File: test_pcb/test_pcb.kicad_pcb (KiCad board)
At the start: 2 copper layers, 67 parts, among them K0 KEYSW, K1 KEYSW, K10 KEYSW, K12 KEYSW, K13 KEYSW, K14 KEYSW, K15 KEYSW, K16 KEYSW, K17 KEYSW, K18 KEYSW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

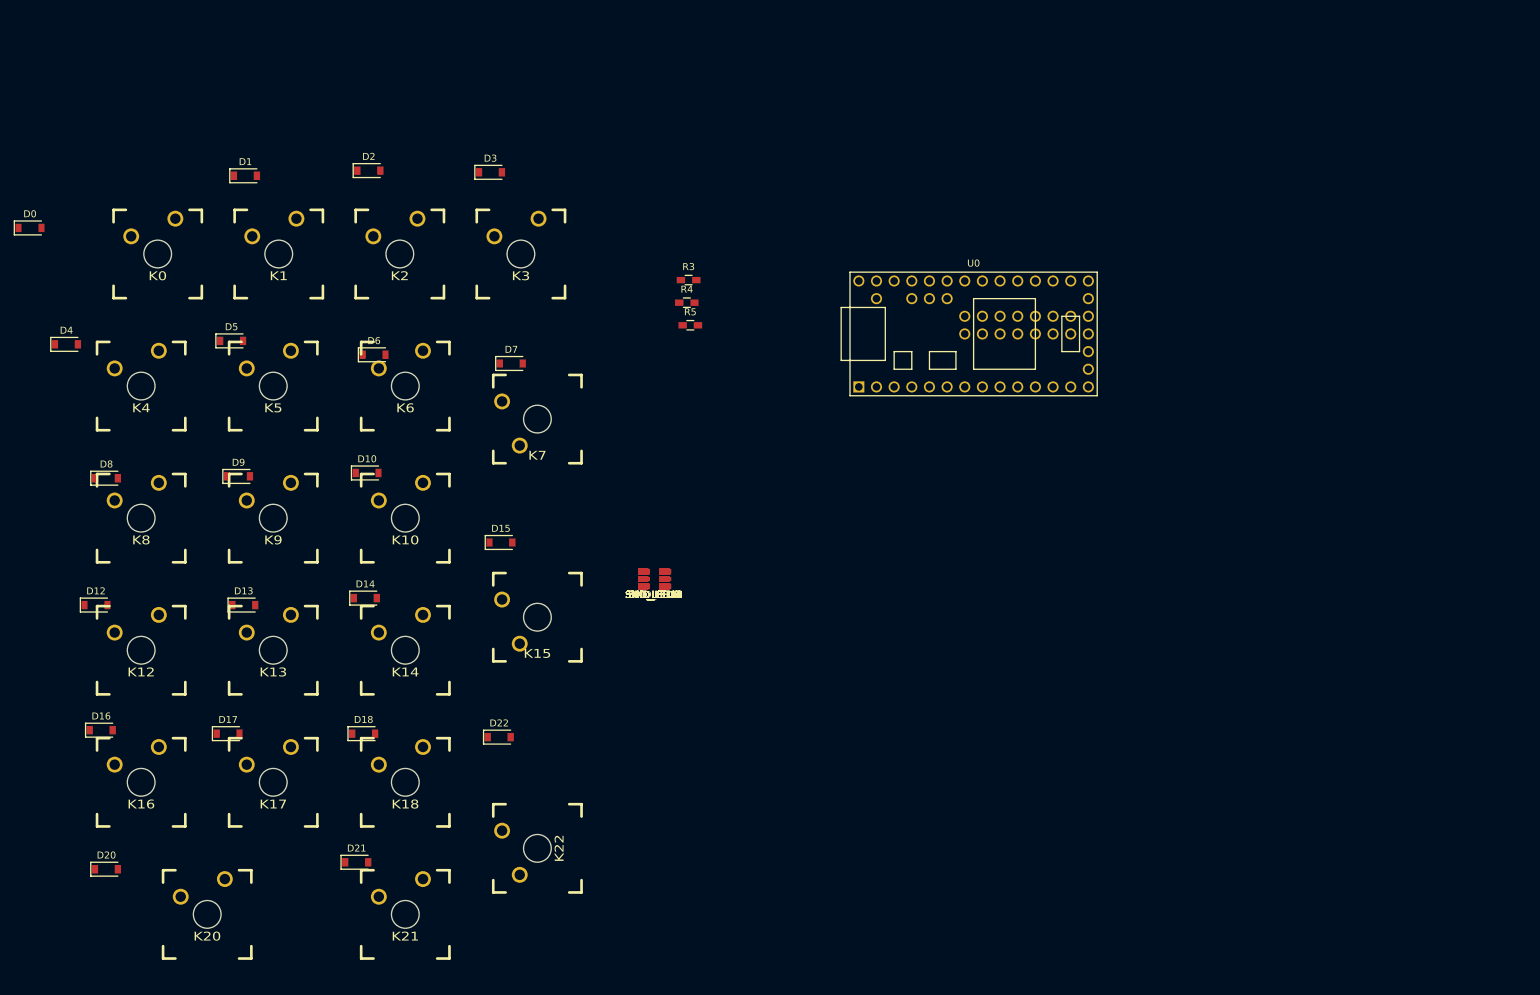
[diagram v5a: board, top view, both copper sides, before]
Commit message: lots of progress on numpad
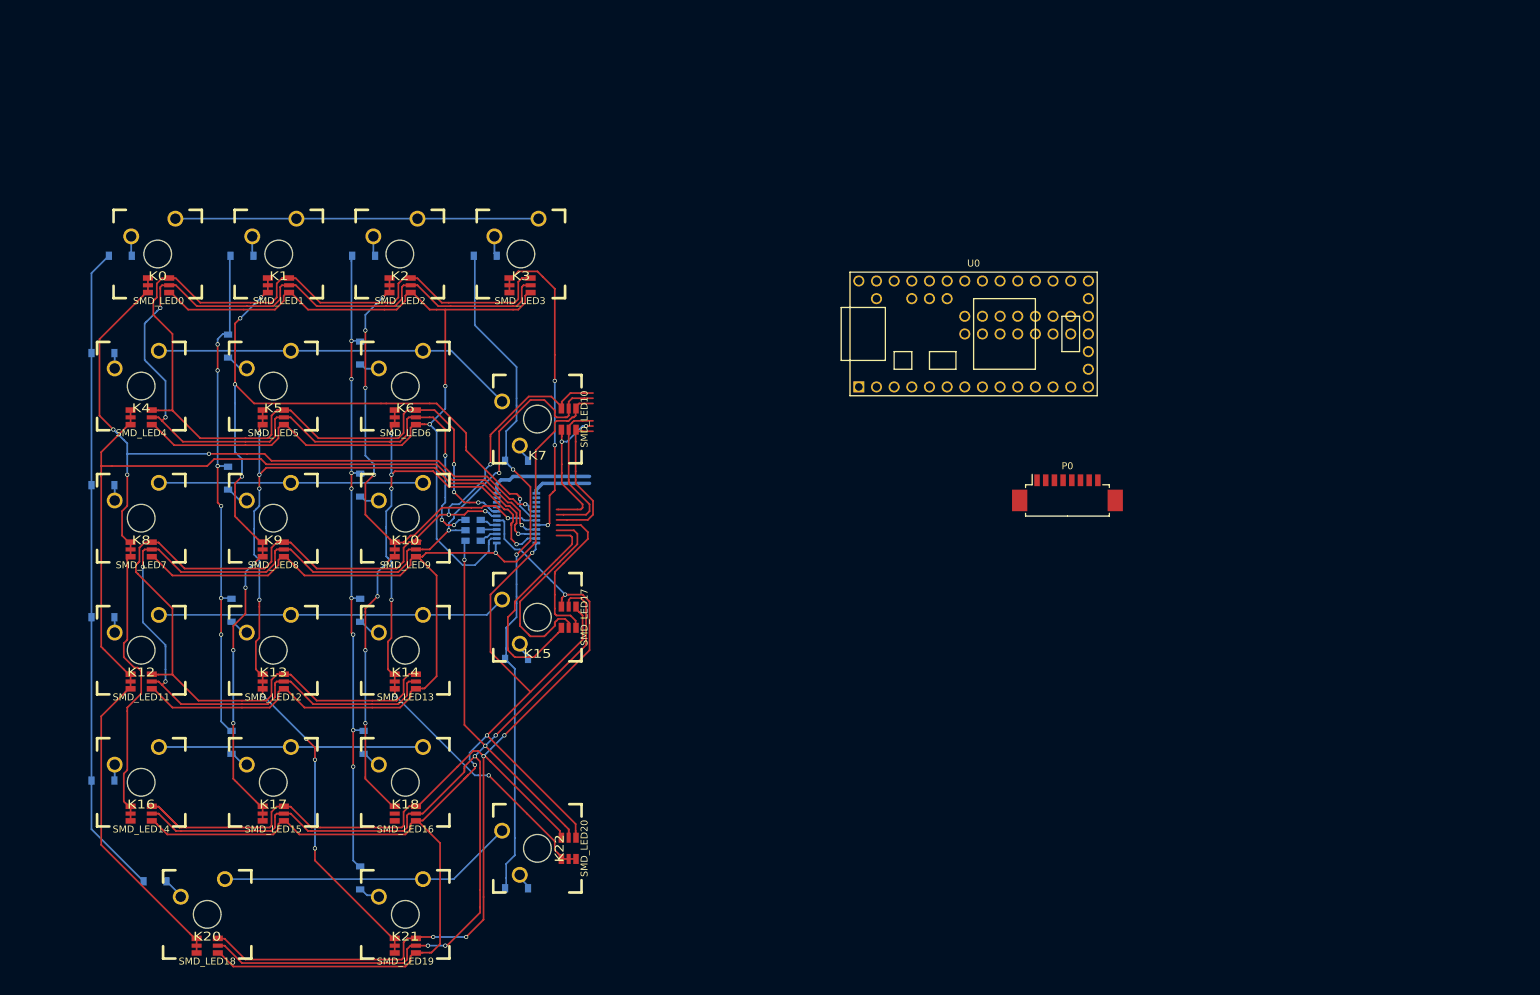
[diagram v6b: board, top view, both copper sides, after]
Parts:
- removed R3, R4, R5: R, Resistors_SMD:R_0603_HandSoldering
- removed SMD_LED21: SMLVN6RGB, cherry_rgb:SMLVN6RGB
- added P0: CONN_01X08, Connectors_Molex:Molex_PicoBlade_53261-0871_08x1.25mm_Angled, F.Cu at (203.2, 85.0)
- added R0: R, Resistors_SMD:R_0603_HandSoldering, B.Cu at (117.8, 89.2)
- added R1: R, Resistors_SMD:R_0603_HandSoldering, B.Cu at (117.8, 90.8)
- added R2: R, Resistors_SMD:R_0603_HandSoldering, B.Cu at (117.8, 92.2)
- added SMD_LED0: SMLVN6RGB, cherry_rgb:SMLVN6RGB, F.Cu at (72.5, 55.5)
- added U1: STP16CP05, Housings_SSOP:TSSOP-24_4.4x7.8mm_Pitch0.65mm, B.Cu at (124.0, 89.0)
- D0, D1, D10, D12, D13, D14, D15, D16, D17, D18, D2, D20, D21, D22, D3, D4, D5, D6, D7, D8, D9: moved to B.Cu
- moved SMD_LED18 83.1 mm to (79.5, 150.5)
- moved SMD_LED14 81.1 mm to (70.0, 131.5)
- moved SMD_LED4 77.3 mm to (70.0, 74.5)
- moved SMD_LED11 75.2 mm to (70.0, 112.5)
- moved SMD_LED7 73.9 mm to (70.0, 93.5)
- moved SMD_LED1 68.8 mm to (89.8, 55.5)
- moved SMD_LED15 64.3 mm to (89.0, 131.5)
- moved SMD_LED19 63.7 mm to (108.0, 150.5)
- moved SMD_LED5 59.5 mm to (89.0, 74.5)
- moved SMD_LED12 56.7 mm to (89.0, 112.5)
- moved SMD_LED2 55.8 mm to (107.2, 55.5)
- moved SMD_LED8 54.9 mm to (89.0, 93.5)
- moved SMD_LED16 49.2 mm to (108.0, 131.5)
- moved SMD_LED3 46.4 mm to (124.5, 55.5)
- moved SMD_LED6 42.6 mm to (108.0, 74.5)
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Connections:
- net Net-(SMD_LED10-Pad1) renamed a3-10-0
- net Net-(SMD_LED10-Pad2) renamed a3-10-1
- net Net-(SMD_LED10-Pad3) renamed a3-10-2
- net Net-(SMD_LED17-Pad1) renamed a3-17-0
- net Net-(SMD_LED17-Pad2) renamed a3-17-1
- net Net-(SMD_LED17-Pad3) renamed a3-17-2
- D0 pad 1: Net-(D0-Pad1) -> c0
- D1 pad 1: Net-(D1-Pad1) -> c1
- D10 pad 1: Net-(D10-Pad1) -> c2
- D12 pad 1: Net-(D12-Pad1) -> c0
- D13 pad 1: Net-(D13-Pad1) -> c1
- D14 pad 1: Net-(D14-Pad1) -> c2
- D15 pad 1: Net-(D15-Pad1) -> c3
- D16 pad 1: Net-(D16-Pad1) -> c0
- D17 pad 1: Net-(D17-Pad1) -> c1
- D18 pad 1: Net-(D18-Pad1) -> c2
- D2 pad 1: Net-(D2-Pad1) -> c2
- D20 pad 1: Net-(D20-Pad1) -> c0
- D21 pad 1: Net-(D21-Pad1) -> c2
- D22 pad 1: Net-(D22-Pad1) -> c3
- D3 pad 1: Net-(D3-Pad1) -> c3
- D4 pad 1: Net-(D4-Pad1) -> c0
- D5 pad 1: Net-(D5-Pad1) -> c1
- D6 pad 1: Net-(D6-Pad1) -> c2
- D7 pad 1: Net-(D7-Pad1) -> c3
- D8 pad 1: Net-(D8-Pad1) -> c0
- D9 pad 1: Net-(D9-Pad1) -> c1
- SMD_LED1 pad 1: Net-(SMD_LED1-Pad1) -> a1
- SMD_LED1 pad 2: Net-(SMD_LED1-Pad2) -> a1
- SMD_LED1 pad 3: Net-(SMD_LED1-Pad3) -> a1
- SMD_LED11 pad 1: Net-(SMD_LED11-Pad1) -> a4
- SMD_LED11 pad 2: Net-(SMD_LED11-Pad2) -> a4
- SMD_LED11 pad 3: Net-(SMD_LED11-Pad3) -> a4
- SMD_LED12 pad 1: Net-(SMD_LED12-Pad1) -> a5
- SMD_LED12 pad 2: Net-(SMD_LED12-Pad2) -> a5
- SMD_LED12 pad 3: Net-(SMD_LED12-Pad3) -> a5
- SMD_LED13 pad 1: Net-(SMD_LED13-Pad1) -> a6
- SMD_LED13 pad 2: Net-(SMD_LED13-Pad2) -> a6
- SMD_LED13 pad 3: Net-(SMD_LED13-Pad3) -> a6
- SMD_LED14 pad 1: Net-(SMD_LED14-Pad1) -> a0
- SMD_LED14 pad 2: Net-(SMD_LED14-Pad2) -> a0
- SMD_LED14 pad 3: Net-(SMD_LED14-Pad3) -> a0
- SMD_LED14 pad 4: green1 -> green2
- SMD_LED14 pad 5: red1 -> red2
- SMD_LED14 pad 6: blue1 -> blue2
- SMD_LED15 pad 1: Net-(SMD_LED15-Pad1) -> a1
- SMD_LED15 pad 2: Net-(SMD_LED15-Pad2) -> a1
- SMD_LED15 pad 3: Net-(SMD_LED15-Pad3) -> a1
- SMD_LED16 pad 1: Net-(SMD_LED16-Pad1) -> a2
- SMD_LED16 pad 2: Net-(SMD_LED16-Pad2) -> a2
- SMD_LED16 pad 3: Net-(SMD_LED16-Pad3) -> a2
- SMD_LED18 pad 1: Net-(SMD_LED18-Pad1) -> a4
- SMD_LED18 pad 2: Net-(SMD_LED18-Pad2) -> a4
- SMD_LED18 pad 3: Net-(SMD_LED18-Pad3) -> a4
- SMD_LED19 pad 1: Net-(SMD_LED19-Pad1) -> a5
- SMD_LED19 pad 2: Net-(SMD_LED19-Pad2) -> a5
- SMD_LED19 pad 3: Net-(SMD_LED19-Pad3) -> a5
- SMD_LED2 pad 1: Net-(SMD_LED2-Pad1) -> a2
- SMD_LED2 pad 2: Net-(SMD_LED2-Pad2) -> a2
- SMD_LED2 pad 3: Net-(SMD_LED2-Pad3) -> a2
- SMD_LED20 pad 1: Net-(SMD_LED20-Pad1) -> a6
- SMD_LED20 pad 2: Net-(SMD_LED20-Pad2) -> a6
- SMD_LED20 pad 3: Net-(SMD_LED20-Pad3) -> a6
- SMD_LED3 pad 1: Net-(SMD_LED3-Pad1) -> a3
- SMD_LED3 pad 2: Net-(SMD_LED3-Pad2) -> a3
- SMD_LED3 pad 3: Net-(SMD_LED3-Pad3) -> a3
- SMD_LED4 pad 1: Net-(SMD_LED4-Pad1) -> a4
- SMD_LED4 pad 2: Net-(SMD_LED4-Pad2) -> a4
- SMD_LED4 pad 3: Net-(SMD_LED4-Pad3) -> a4
- SMD_LED5 pad 1: Net-(SMD_LED5-Pad1) -> a5
- SMD_LED5 pad 2: Net-(SMD_LED5-Pad2) -> a5
- SMD_LED5 pad 3: Net-(SMD_LED5-Pad3) -> a5
- SMD_LED6 pad 1: Net-(SMD_LED6-Pad1) -> a6
- SMD_LED6 pad 2: Net-(SMD_LED6-Pad2) -> a6
- SMD_LED6 pad 3: Net-(SMD_LED6-Pad3) -> a6
- SMD_LED7 pad 1: Net-(SMD_LED7-Pad1) -> a0
- SMD_LED7 pad 2: Net-(SMD_LED7-Pad2) -> a0
- SMD_LED7 pad 3: Net-(SMD_LED7-Pad3) -> a0
- SMD_LED7 pad 4: green0 -> green1
- SMD_LED7 pad 5: red0 -> red1
- SMD_LED7 pad 6: blue0 -> blue1
- SMD_LED8 pad 1: Net-(SMD_LED8-Pad1) -> a1
- SMD_LED8 pad 2: Net-(SMD_LED8-Pad2) -> a1
- SMD_LED8 pad 3: Net-(SMD_LED8-Pad3) -> a1
- SMD_LED9 pad 1: Net-(SMD_LED9-Pad1) -> a2
- SMD_LED9 pad 2: Net-(SMD_LED9-Pad2) -> a2
- SMD_LED9 pad 3: Net-(SMD_LED9-Pad3) -> a2
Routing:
- net red2: track 0.00 -> 205.7 mm, vias 0 -> 6
- net blue2: track 0.00 -> 196.2 mm, vias 0 -> 5
- net green2: track 0.00 -> 188.1 mm, vias 0 -> 3
- net blue1: track 0.00 -> 165.7 mm, vias 0 -> 3
- net a4: track 0.00 -> 160.0 mm, vias 0 -> 1
- net blue0: track 0.00 -> 158.2 mm, vias 0 -> 3
- net red1: track 0.00 -> 158.2 mm, vias 0 -> 4
- net green1: track 0.00 -> 155.5 mm, vias 0 -> 1
- net red0: track 0.00 -> 155.0 mm, vias 0 -> 5
- net green0: track 0.00 -> 153.7 mm, vias 0 -> 2
- net a0: track 0.00 -> 152.0 mm, vias 0 -> 4
- net a1: track 0.00 -> 143.5 mm, vias 0 -> 9
- net a5: track 0.00 -> 135.7 mm, vias 0 -> 9
- net a6: track 0.00 -> 110.7 mm, vias 0 -> 7
- net a2: track 0.00 -> 108.6 mm, vias 0 -> 9
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
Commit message: ground planes added
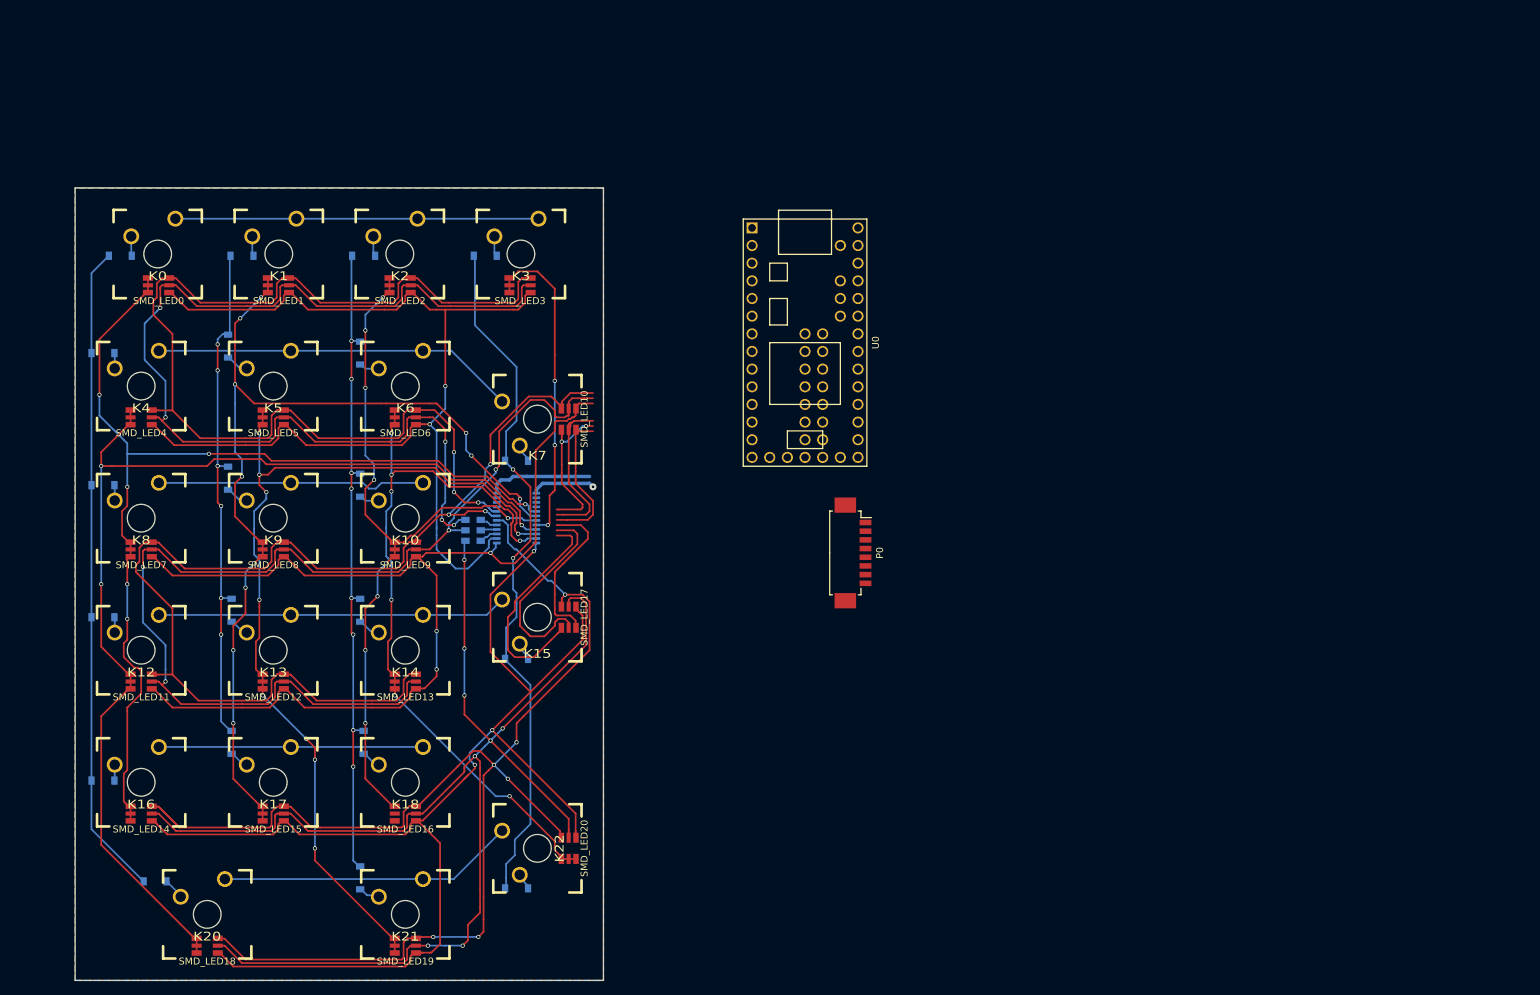
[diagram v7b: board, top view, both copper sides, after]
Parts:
- moved P0 31.8 mm to (172.8, 94.0), turned to 270 degrees
- moved U0 24.3 mm to (165.5, 63.8), turned to 270 degrees
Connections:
- U1 pad 1: Net-(U1-Pad1) -> GND
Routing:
- net GND: track 0.00 -> 9.45 mm, vias 0 -> 1
- net Net-(U1-Pad1): track 8.75 -> 0.00 mm
- net a3-10-1: track 23.0 -> 26.3 mm
- net c3: track 100.0 -> 102.3 mm
- net red2: track 205.7 -> 207.1 mm, vias 6 -> 8
- net blue2: track 196.2 -> 197.3 mm, vias 5 -> 6
- net green0: track 153.7 -> 154.7 mm
- net a5: track 135.7 -> 136.6 mm
- net a6: track 110.7 -> 110.0 mm
- net r2: track 38.0 -> 38.7 mm
- net blue1: track 165.7 -> 165.1 mm
- net green1: track 155.5 -> 156.0 mm, vias 1 -> 3
- net a0: vias 4 -> 6
- net a4: vias 1 -> 3
- net a1: vias 9 -> 11
- added copper zone on B.Cu, net GND
- added copper zone on F.Cu, net GND
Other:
- board outline added: 76 x 114 mm

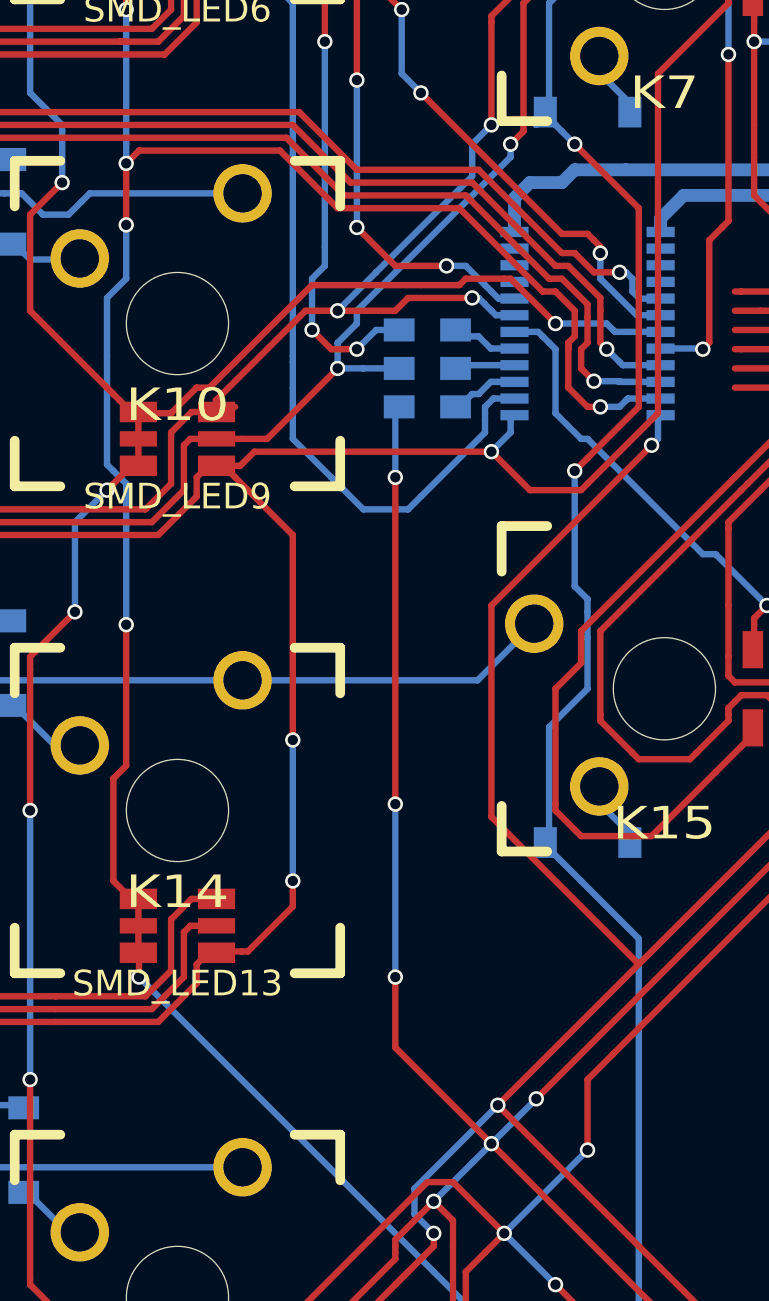
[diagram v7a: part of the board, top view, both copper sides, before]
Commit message: when you use a contant current LED driver you don't actually need resistors!
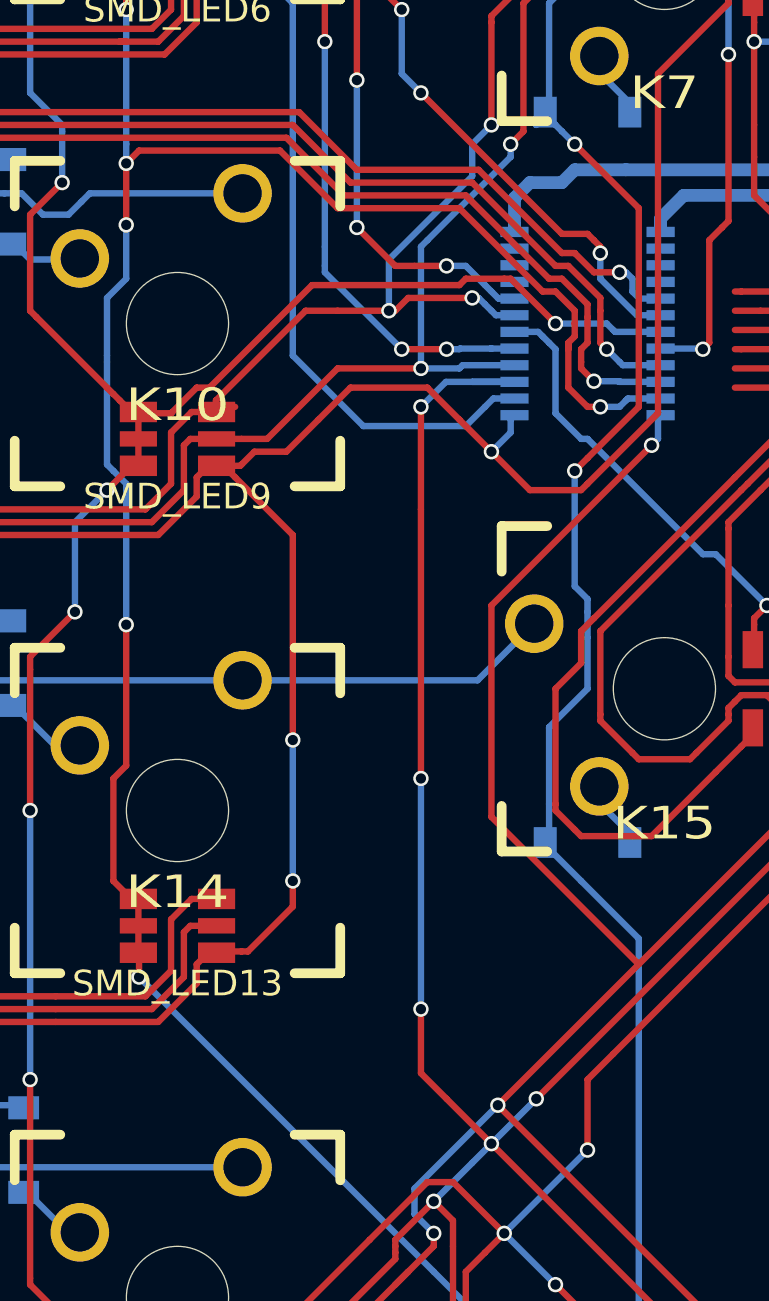
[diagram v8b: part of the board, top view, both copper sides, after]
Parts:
- removed R0, R1, R2: R, Resistors_SMD:R_0603_HandSoldering
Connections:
- U1 pad 15: Net-(R2-Pad1) -> red2
- U1 pad 16: Net-(R1-Pad1) -> red1
- U1 pad 17: Net-(R0-Pad1) -> red0
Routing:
- net red2: track 207.1 -> 212.3 mm
- net green0: track 154.7 -> 149.5 mm
- net red1: track 157.9 -> 161.1 mm
- net Net-(R2-Pad1): track 2.97 -> 0.00 mm
- net Net-(R0-Pad1): track 2.57 -> 0.00 mm
- net Net-(R1-Pad1): track 2.55 -> 0.00 mm
- net red0: track 155.0 -> 157.2 mm
- net green1: track 156.0 -> 158.1 mm
- net blue1: track 165.1 -> 164.3 mm
